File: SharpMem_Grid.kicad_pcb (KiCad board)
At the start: 2 copper layers, 31 x 36 mm, 31 parts, among them J1 CONN_01X05, P1 USB_B, P2 CONN_02X04, SW1 PTS810_SJK_250_SMTR_LFS, SW2 PTS810_SJK_250_SMTR_LFS, U1 25LC_EEPROM, U2 Schmitt_Inverter_Single, U3 PIC32MX250F128B-I/SS, Y1 ABLS-8.000MHZ-B4-T

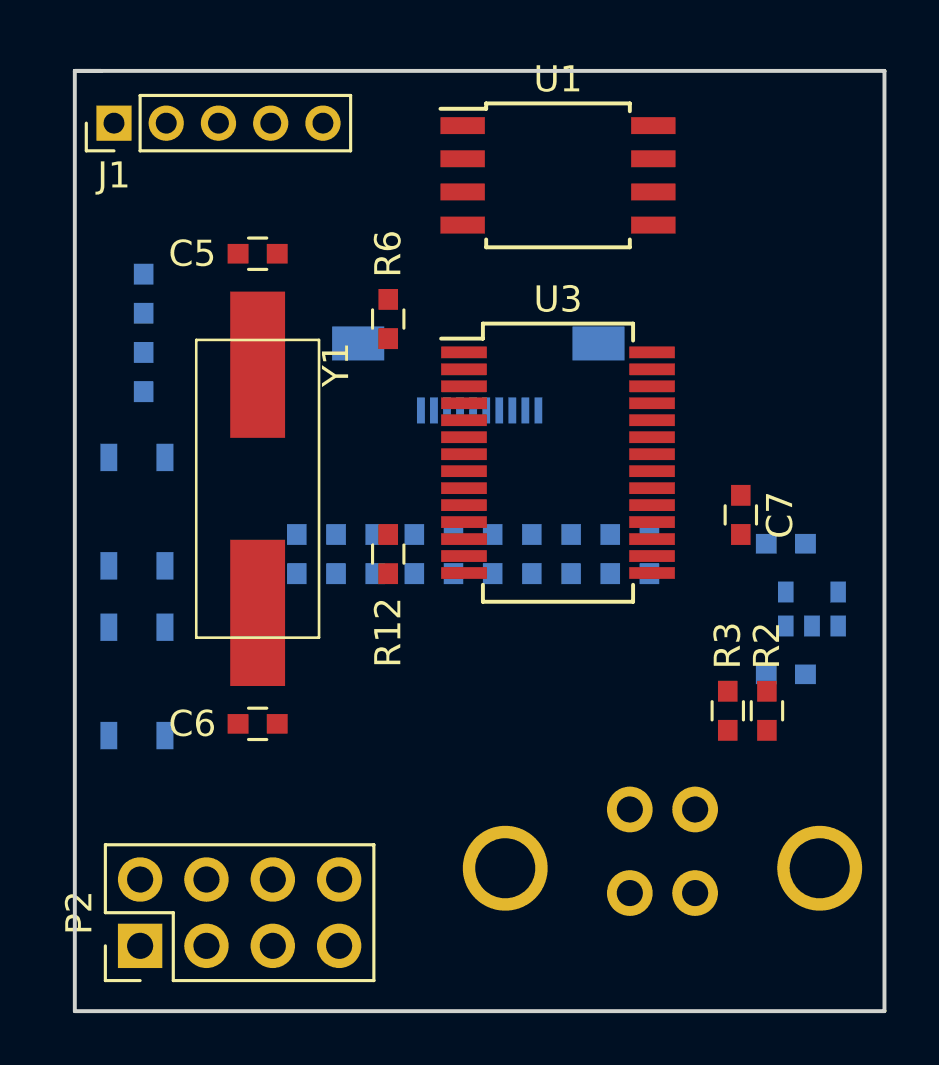
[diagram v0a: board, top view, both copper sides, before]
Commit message: Routed traces and copper pour. Passes DFM
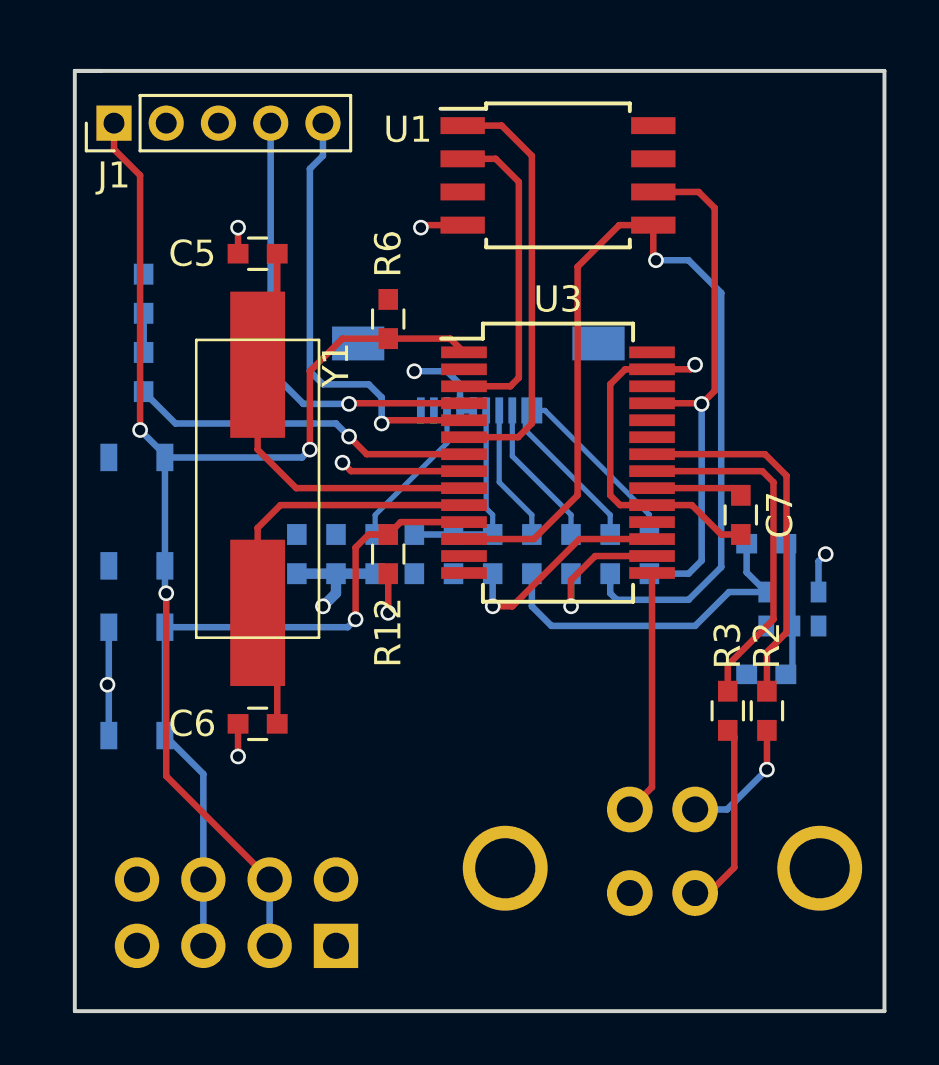
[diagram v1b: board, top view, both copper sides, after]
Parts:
- P2: moved to B.Cu
- moved P2 7.50 mm to (46.0, 111.5)
- moved C1 0.75 mm to (62.5, 101.1)
- moved R1 0.75 mm to (62.5, 96.1)
- moved U2 0.75 mm to (63.5, 98.6)
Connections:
- P1 pad 6: (no net) -> GND
- U3 pad 16: Net-(U3-Pad16) -> /LCD_SS
- U3 pad 17: Net-(U3-Pad17) -> /DISP
- U3 pad 2: /EE_SS -> Net-(U3-Pad2)
- U3 pad 26: /DISP -> Net-(U3-Pad26)
- U3 pad 6: /LCD_SS -> /EE_SS
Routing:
- net /MCLR: track 0.00 -> 50.8 mm, vias 0 -> 3
- net /MOSI: track 0.00 -> 37.9 mm, vias 0 -> 1
- net /PROG: track 0.00 -> 27.5 mm, vias 0 -> 1
- net GND: track 0.00 -> 23.9 mm, vias 0 -> 6
- net /SCLK: track 0.00 -> 20.5 mm, vias 0 -> 1
- net /PGD: track 0.00 -> 17.4 mm, vias 0 -> 1
- net /PGC: track 0.00 -> 17.1 mm, vias 0 -> 1
- net Net-(C5-Pad1): track 0.00 -> 16.3 mm
- net /EE_SS: track 0.00 -> 16.2 mm
- net Net-(C6-Pad1): track 0.00 -> 16.1 mm
- net /D-: track 0.00 -> 14.1 mm
- net +3V3: track 0.00 -> 13.7 mm, vias 0 -> 4
- net /D+: track 0.00 -> 13.6 mm
- net /LED: track 0.00 -> 13.3 mm, vias 0 -> 1
- net /EXTCOMIN: track 0.00 -> 13.2 mm
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- added copper zone on F.Cu, net +3V3
- added copper zone on B.Cu, net GND

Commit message: Final layout and BOM
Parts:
- added J2: CONN_01X01, Solutions:NPT_125mil, F.Cu at (196.0, 111.2)
- added J3: CONN_01X01, Solutions:NPT_125mil, F.Cu at (158.0, 82.2)
- Y1: value ABLS-8.000MHZ-B4-T -> ECS-080-18-23G-JGN-TR; footprint Solutions:ABLS_SMT_XTAL -> Solutions:ECS-080-18-23G-JGN-TR_8MHz_60x35
- moved P2 126.2 mm to (172.0, 105.0), turned to 180 degrees
- moved D1 125.6 mm to (164.2, 88.2)
- moved R13 125.6 mm to (164.2, 85.5)
- moved C5 125.6 mm to (168.5, 89.8)
- moved C6 125.5 mm to (168.5, 99.8)
- moved SW2 125.5 mm to (163.5, 99.0)
- moved SW1 125.5 mm to (163.5, 92.8)
- moved C1 125.5 mm to (188.0, 101.9)
- moved C2 125.5 mm to (170.0, 97.2)
- moved C3 125.5 mm to (171.5, 97.2)
- moved C4 125.5 mm to (174.5, 97.2)
- moved C7 125.5 mm to (187.0, 95.8)
- moved DIS1 125.5 mm to (177.0, 91.8)
- moved J1 125.5 mm to (163.0, 80.8)
- moved P1 125.5 mm to (184.0, 108.6)
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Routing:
- net /PROG: track 27.5 -> 35.6 mm
- net Net-(C5-Pad1): track 16.3 -> 11.6 mm
- net Net-(C6-Pad1): track 16.1 -> 11.6 mm
- net /MCLR: track 50.8 -> 49.7 mm
- net +3V3: track 13.7 -> 14.7 mm
- net /LED: track 13.3 -> 14.0 mm
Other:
- board size 31 x 36 mm -> 45 x 36 mm
- board text added: "1/8" Dia Hole"

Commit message: redesighn for itp camp
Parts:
- removed P1: USB_B, Solutions:USB_B_VERTICAL
- removed P2: CONN_02X04, Pin_Headers:Pin_Header_Straight_2x04_Pitch2.54mm
- added BT1: Battery_Cell, Solutions:4UCON-0217-20519, B.Cu at (184.8, 109.7)
- added C8: 1uF, Capacitors_SMD:C_0603, F.Cu at (189.2, 88.2)
- added C9: 1uF, Capacitors_SMD:C_0603, F.Cu at (189.2, 83.2)
- added D2: DIODE, Diodes_SMD:D_0603, F.Cu at (183.8, 109.7)
- added D3: DIODE, Diodes_SMD:D_0603, F.Cu at (184.4, 107.0)
- added J4: USB_B_Micro, Solutions:10118193_microUSB, B.Cu at (191.1, 96.7)
- added U4: TLV76033DBZR, TO_SOT_Packages_SMD:SOT-23, F.Cu at (189.4, 85.7)
- added U5: MCP73831-2-OT, TO_SOT_Packages_SMD:SOT-23-5, F.Cu at (186.2, 109.6)
- J2, J3: footprint Solutions:NPT_125mil -> Mounting_Holes:MountingHole_3.2mm_M3
- R10: moved to F.Cu
- R13: value 10K -> 220R
- R4, R5, R7, R8, R9: value 220 -> 220R
- moved SW2 28.4 mm to (190.0, 109.2)
- moved SW1 28.3 mm to (190.2, 83.3)
- moved U2 21.3 mm to (167.7, 98.2), turned to 270 degrees
- moved C1 20.3 mm to (168.7, 95.7), turned to 180 degrees
- moved R10 20.1 mm to (186.2, 112.3), turned to 180 degrees
- moved R1 19.7 mm to (168.7, 100.7), turned to 0 degrees
- moved J1 19.4 mm to (163.3, 100.2), turned to 180 degrees
- moved C2 12.3 mm to (182.2, 95.8), turned to 270 degrees
- moved R4 11.8 mm to (171.8, 95.8)
- moved C3 9.50 mm to (180.9, 95.8), turned to 270 degrees
- moved R5 9.01 mm to (173.1, 95.8)
- moved U3 8.30 mm to (176.0, 101.0)
- moved R7 6.26 mm to (174.4, 95.8)
- moved C4 5.29 mm to (179.6, 95.8)
- moved U1 4.53 mm to (177.0, 86.2)
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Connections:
- D1 pad 2: /LED -> /PGD
- DIS1 pad 1: GND -> Net-(DIS1-Pad1)
- DIS1 pad 10: Net-(DIS1-Pad10) -> GND
- DIS1 pad 2: GND -> Net-(DIS1-Pad2)
- DIS1 pad 4: +3V3 -> Net-(DIS1-Pad4)
- DIS1 pad 5: +3V3 -> Net-(C4-Pad1)
- DIS1 pad 6: Net-(C4-Pad1) -> +3V3
- DIS1 pad 7: Net-(DIS1-Pad7) -> +3V3
- DIS1 pad 8: Net-(DIS1-Pad8) -> +3V3
- DIS1 pad 9: Net-(DIS1-Pad9) -> GND
- R10 pad 1: Net-(DIS1-Pad3) -> Net-(R10-Pad1)
- R10 pad 2: +3V3 -> GND
- R2 pad 1: /D- -> /D+
- R3 pad 1: /D+ -> /D-
- R4 pad 1: Net-(DIS1-Pad10) -> Net-(DIS1-Pad1)
- R5 pad 1: Net-(DIS1-Pad9) -> Net-(DIS1-Pad2)
- R7 pad 1: Net-(DIS1-Pad8) -> Net-(DIS1-Pad3)
- R8 pad 1: Net-(DIS1-Pad7) -> Net-(DIS1-Pad4)
- U3 pad 7: /LED -> Net-(U3-Pad7)
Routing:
- net /MCLR: track 49.7 -> 0.00 mm, vias 3 -> 0
- net /MOSI: track 37.9 -> 0.00 mm, vias 1 -> 0
- net /PROG: track 35.6 -> 0.00 mm, vias 1 -> 0
- net /SCLK: track 20.5 -> 0.00 mm, vias 1 -> 0
- net /PGC: track 17.1 -> 0.00 mm, vias 1 -> 0
- net /EE_SS: track 16.2 -> 0.00 mm
- net /D-: track 14.1 -> 0.00 mm
- net /LED: track 14.0 -> 0.00 mm, vias 1 -> 0
- net /D+: track 13.6 -> 0.00 mm
- net +3V3: track 14.7 -> 1.57 mm, vias 4 -> 1
- net /PGD: track 17.4 -> 4.41 mm, vias 1 -> 0
- net /MISO: track 12.3 -> 0.00 mm
- net Net-(C6-Pad1): track 11.6 -> 0.00 mm
- net Net-(C5-Pad1): track 11.6 -> 0.00 mm
- net /EXTCOMIN: track 13.2 -> 2.16 mm
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- removed copper zone on B.Cu, net GND
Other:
- board text added: "Heart Bone"
- board text added: "Solutions Design & Prototyping, Brooklyn www.github.com/biomurph/SharpMem_Grid"

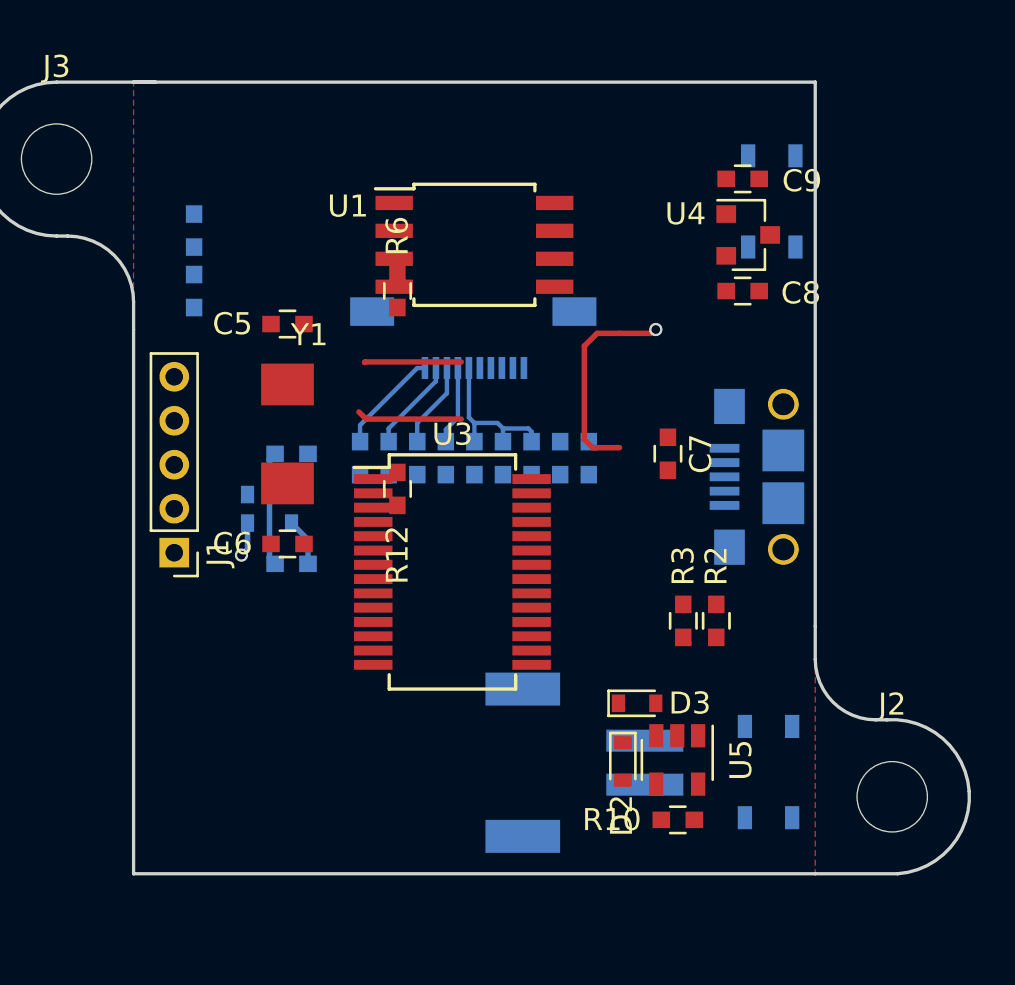
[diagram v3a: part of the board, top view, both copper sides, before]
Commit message: board layout and routing passing DRC
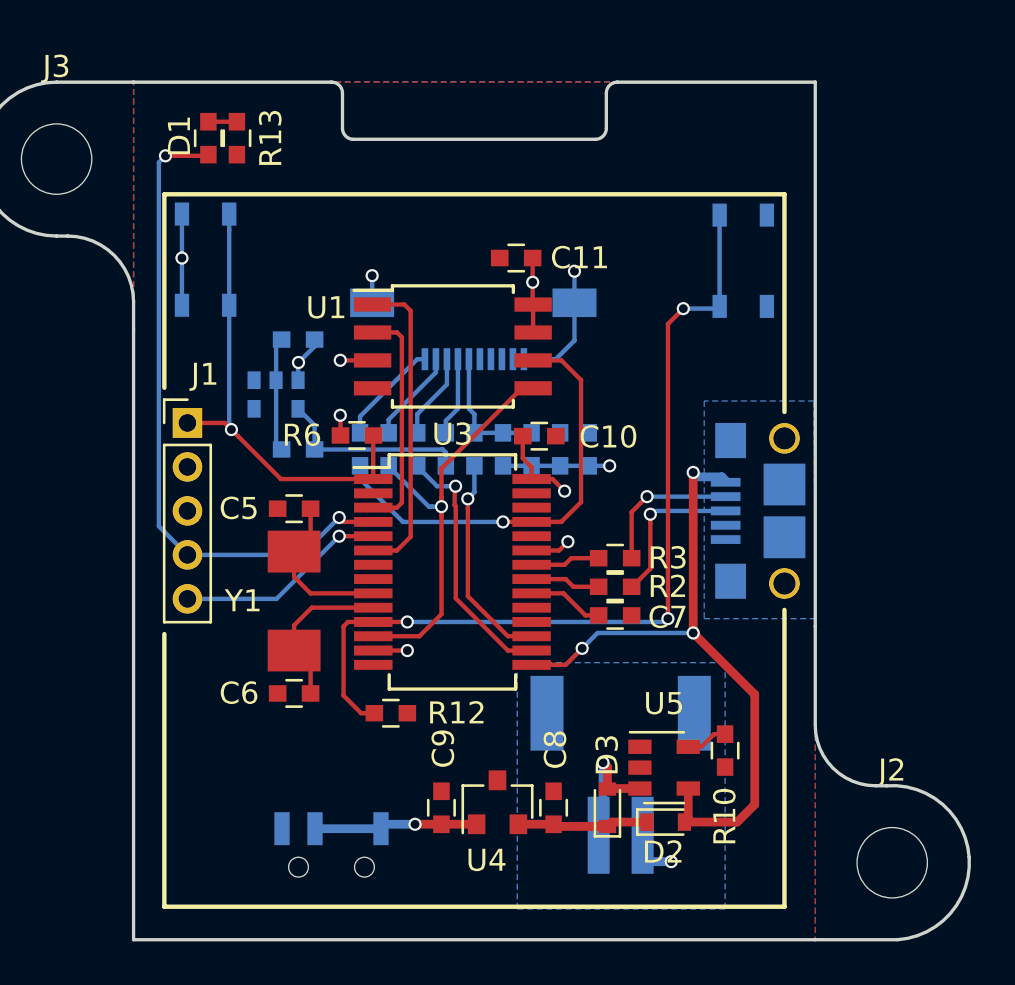
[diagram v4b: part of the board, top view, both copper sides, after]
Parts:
- added C10: 0.1uF, Capacitors_SMD:C_0603, F.Cu at (179.9, 94.8)
- added C11: 0.1uF, Capacitors_SMD:C_0603, F.Cu at (178.9, 86.8)
- added SW3: SW_SPDT, Solutions:SSSS810701_ALPS_SPDT, B.Cu at (170.5, 114.5)
- D1, R13: moved to F.Cu
- U1: value 25LC_EEPROM -> 25LC1024T-I/SM
- moved C9 31.7 mm to (175.5, 111.8), turned to 270 degrees
- moved U4 28.2 mm to (178.1, 111.5), turned to 90 degrees
- moved SW1 25.9 mm to (164.4, 86.0)
- moved C8 25.0 mm to (180.6, 111.8), turned to 90 degrees
- moved SW2 21.5 mm to (189.6, 87.8), turned to 90 degrees
- moved R12 10.2 mm to (173.2, 107.5), turned to 0 degrees
- moved C5 8.41 mm to (168.8, 98.2)
- moved C7 7.73 mm to (183.4, 103.0), turned to 0 degrees
- moved Y1 7.61 mm to (168.8, 102.3)
- moved D1 6.98 mm to (164.9, 81.3)
- moved R6 6.82 mm to (171.7, 94.8), turned to 180 degrees
- moved C6 6.81 mm to (168.8, 106.5)
- moved J1 5.93 mm to (163.9, 94.2), turned to 0 degrees
- moved C1 5.21 mm to (169.0, 90.5)
- moved R1 5.21 mm to (169.0, 95.5)
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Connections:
- BT1 pad 3: (no net) -> GND
- BT1 pad 4: (no net) -> GND
- J4 pad 10: (no net) -> GND
- J4 pad 11: (no net) -> GND
- J4 pad 7: (no net) -> GND
- J4 pad 8: (no net) -> GND
- J4 pad 9: (no net) -> GND
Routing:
- net /PROG: track 0.00 -> 40.0 mm, vias 0 -> 3
- net /V_USB: track 0.00 -> 31.0 mm, vias 0 -> 3
- net /PGD: track 4.41 -> 30.0 mm, vias 0 -> 2
- net /MCLR: track 0.00 -> 21.3 mm, vias 0 -> 1
- net /SCLK: track 0.00 -> 19.9 mm, vias 0 -> 1
- net /MOSI: track 0.00 -> 19.0 mm, vias 0 -> 1
- net /EE_SS: track 0.00 -> 14.1 mm
- net /LCD_SS: track 0.00 -> 11.7 mm, vias 0 -> 1
- net +3V3: track 1.57 -> 13.0 mm, vias 1 -> 6
- net /MISO: track 0.00 -> 10.3 mm
- net /DISP: track 0.00 -> 9.71 mm, vias 0 -> 1
- net /PGC: track 0.00 -> 9.63 mm, vias 0 -> 1
- net Net-(C9-Pad2): track 0.00 -> 7.43 mm, vias 0 -> 1
- net Net-(C6-Pad1): track 0.00 -> 7.34 mm
- net Net-(C5-Pad1): track 0.00 -> 7.32 mm
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- added copper zone on B.Cu, net +3V3
- added copper zone on B.Cu, net GND
- added copper zone on F.Cu, net GND
- removed copper zone on F.Cu, net +3V3
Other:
- board size 45 x 36 mm -> 45 x 39 mm
- board text added: "Flywheel Lab, Brooklyn"
- board text added: "PROG"
- board text added: "RESET"
- board text removed: "Solutions Design & Prototyping, Brooklyn www.github.com/biomurph/SharpMem_Grid"

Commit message: dusting up and moving to new repo
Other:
- outline, holes or cut-outs redrawn
- board text added: "line for V score"
- board text removed: "1/8" Dia Hole"
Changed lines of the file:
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@@
   (general
     (thickness 1.6)
-    (drawings 50)
-    (tracks 244)
+    (drawings 57)
+    (tracks 242)
     (zones 0)
     (modules 42)
@@
     (40 Dwgs.User user hide)
     (41 Cmts.User user hide)
-    (42 Eco1.User user hide)
+    (42 Eco1.User user)
     (43 Eco2.User user)
     (44 Edge.Cuts user)
@@
   )
   (setup
-    (last_trace_width 0.2)
+    (last_trace_width 0.25)
     (user_trace_width 0.2)
     (user_trace_width 0.3)
@@
     (pad "" np_thru_hole circle (at 0 1.5 90) (size 0.9 0.9) (drill 0.9) (layers *.Cu *.Mask B.SilkS))
   )
+  (gr_line (start 161.55 78.35) (end 161.3 77.75) (layer Eco2.User) (width 0.2))
+  (gr_line (start 162.55 75.4) (end 161.55 78.35) (layer Eco2.User) (width 0.2))
+  (gr_text "line for V score" (at 171.9 75.35) (layer Eco2.User)
+    (effects (font (size 1.5 1.5) (thickness 0.3)))
+  )
+  (gr_line (start 192.45 118.2) (end 192.75 118.85) (layer Eco2.User) (width 0.2))
+  (gr_line (start 191.65 121.9) (end 192.45 118.2) (layer Eco2.User) (width 0.2))
+  (gr_text "line for V score" (at 182.05 121.8) (layer Eco2.User)
+    (effects (font (size 1.5 1.5) (thickness 0.3)))
+  )
+  (gr_line (start 192.5 117.75) (end 192.5 107.95) (layer Edge.Cuts) (width 0.15))
+  (gr_line (start 161.5 78.75) (end 161.5 88.65) (layer Edge.Cuts) (width 0.15))
   (gr_text PROG (at 188.5 82.35 180) (layer B.SilkS)
     (effects (font (size 1.5 1.5) (thickness 0.3)) (justify mirror))
@@
   (gr_text "Flywheel Lab, Brooklyn" (at 177 104.95 180) (layer B.SilkS)
     (effects (font (size 1 1) (thickness 0.125)) (justify mirror))
-  )
-  (gr_text "1/8\" Dia Hole\n" (at 203.5 105) (layer Eco1.User)
-    (effects (font (size 1.5 1.5) (thickness 0.3)))
   )
   (gr_line (start 161.5 88.75) (end 161.5 90) (angle 90) (layer Edge.Cuts) (width 0.15))
@@
   (segment (start 171.8 96.8) (end 173.75 98.75) (width 0.2) (layer B.Cu) (net 15))
   (segment (start 177.87575 98.75) (end 178.300014 98.75) (width 0.2) (layer B.Cu) (net 15))
-  (segment (start 179.145 92.675) (end 175.503763 96.316237) (width 0.2) (layer F.Cu) (net 16))
+  (segment (start 175.499988 102.950012) (end 175.499988 98.479474) (width 0.2) (layer F.Cu) (net 16))
+  (segment (start 175.499988 96.320012) (end 175.499988 97.630946) (width 0.2) (layer F.Cu) (net 16))
+  (via (at 175.499988 98.05521) (size 0.6) (drill 0.4) (layers F.Cu B.Cu) (net 16))
+  (segment (start 174.93021 98.05521) (end 175.075724 98.05521) (width 0.2) (layer B.Cu) (net 16))
   (segment (start 173.1 96.225) (end 174.93021 98.05521) (width 0.2) (layer B.Cu) (net 16))
-  (segment (start 175.503763 102.946237) (end 175.503763 98.479474) (width 0.2) (layer F.Cu) (net 16))
-  (segment (start 174.5 103.95) (end 175.503763 102.946237) (width 0.2) (layer F.Cu) (net 16))
-  (segment (start 175.503763 98.479474) (end 175.503763 98.05521) (width 0.2) (layer F.Cu) (net 16))
-  (segment (start 175.503763 96.316237) (end 175.503763 97.630946) (width 0.2) (layer F.Cu) (net 16))
-  (segment (start 175.079499 98.05521) (end 175.503763 98.05521) (width 0.2) (layer B.Cu) (net 16))
+  (segment (start 173.1 96.2) (end 173.1 96.225) (width 0.2) (layer B.Cu) (net 16))
+  (segment (start 175.499988 97.630946) (end 175.499988 98.05521) (width 0.2) (layer F.Cu) (net 16))
+  (segment (start 175.075724 98.05521) (end 175.499988 98.05521) (width 0.2) (layer B.Cu) (net 16))
+  (segment (start 172.4 103.95) (end 174.5 103.95) (width 0.2) (layer F.Cu) (net 16))
+  (segment (start 174.5 103.95) (end 175.499988 102.950012) (width 0.2) (layer F.Cu) (net 16))
+  (segment (start 175.499988 98.479474) (end 175.499988 98.05521) (width 0.2) (layer F.Cu) (net 16))
   (segment (start 179.67 92.675) (end 179.145 92.675) (width 0.2) (layer F.Cu) (net 16))
-  (segment (start 175.503763 97.630946) (end 175.503763 98.05521) (width 0.2) (layer F.Cu) (net 16))
-  (segment (start 174.93021 98.05521) (end 175.079499 98.05521) (width 0.2) (layer B.Cu) (net 16))
-  (via (at 175.503763 98.05521) (size 0.6) (drill 0.4) (layers F.Cu B.Cu) (net 16))
-  (segment (start 173.1 96.2) (end 173.1 96.225) (width 0.2) (layer B.Cu) (net 16))
-  (segment (start 172.4 103.95) (end 174.5 103.95) (width 0.2) (layer F.Cu) (net 16))
+  (segment (start 179.145 92.675) (end 175.499988 96.320012) (width 0.2) (layer F.Cu) (net 16))
   (segment (start 174.4 96.225) (end 175.301404 97.126404) (width 0.2) (layer B.Cu) (net 17))
   (via (at 176.14232 97.126404) (size 0.6) (drill 0.4) (layers F.Cu B.Cu) (net 17))
   (segment (start 175.301404 97.126404) (end 175.718056 97.126404) (width 0.2) (layer B.Cu) (net 17))
-  (segment (start 179.6 104.6) (end 178.525 104.6) (width 0.2) (layer F.Cu) (net 17))
-  (segment (start 176.149998 98.038002) (end 176.099998 97.988002) (width 0.2) (layer F.Cu) (net 17))
   (segment (start 175.718056 97.126404) (end 176.14232 97.126404) (width 0.2) (layer B.Cu) (net 17))
   (segment (start 174.4 96.2) (end 174.4 96.225) (width 0.2) (layer B.Cu) (net 17))
-  (segment (start 176.149998 102.224998) (end 176.149998 98.038002) (width 0.2) (layer F.Cu) (net 17))
+  (segment (start 178.525 104.6) (end 176.099998 102.174998) (width 0.2) (layer F.Cu) (net 17))
   (segment (start 176.099998 97.168726) (end 176.14232 97.126404) (width 0.2) (layer F.Cu) (net 17))
-  (segment (start 176.099998 97.988002) (end 176.099998 97.168726) (width 0.2) (layer F.Cu) (net 17))
-  (segment (start 178.525 104.6) (end 176.149998 102.224998) (width 0.2) (layer F.Cu) (net 17))
+  (segment (start 176.099998 102.174998) (end 176.099998 97.168726) (width 0.2) (layer F.Cu) (net 17))
+  (segment (start 179.6 104.6) (end 178.525 104.6) (width 0.2) (layer F.Cu) (net 17))
   (segment (start 177 96.2) (end 177 97.399998) (width 0.2) (layer B.Cu) (net 18))
   (segment (start 178.525 103.95) (end 176.699998 102.124998) (width 0.2) (layer F.Cu) (net 18))
